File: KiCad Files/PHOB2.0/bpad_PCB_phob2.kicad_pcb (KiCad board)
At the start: 2 copper layers, 31.6 x 54.4 mm, 25 parts, among them J1 Conn_01x06, SW1 C_left, SW2 C_up, SW3 C_down, SW4 C_right, U1 MCP3202

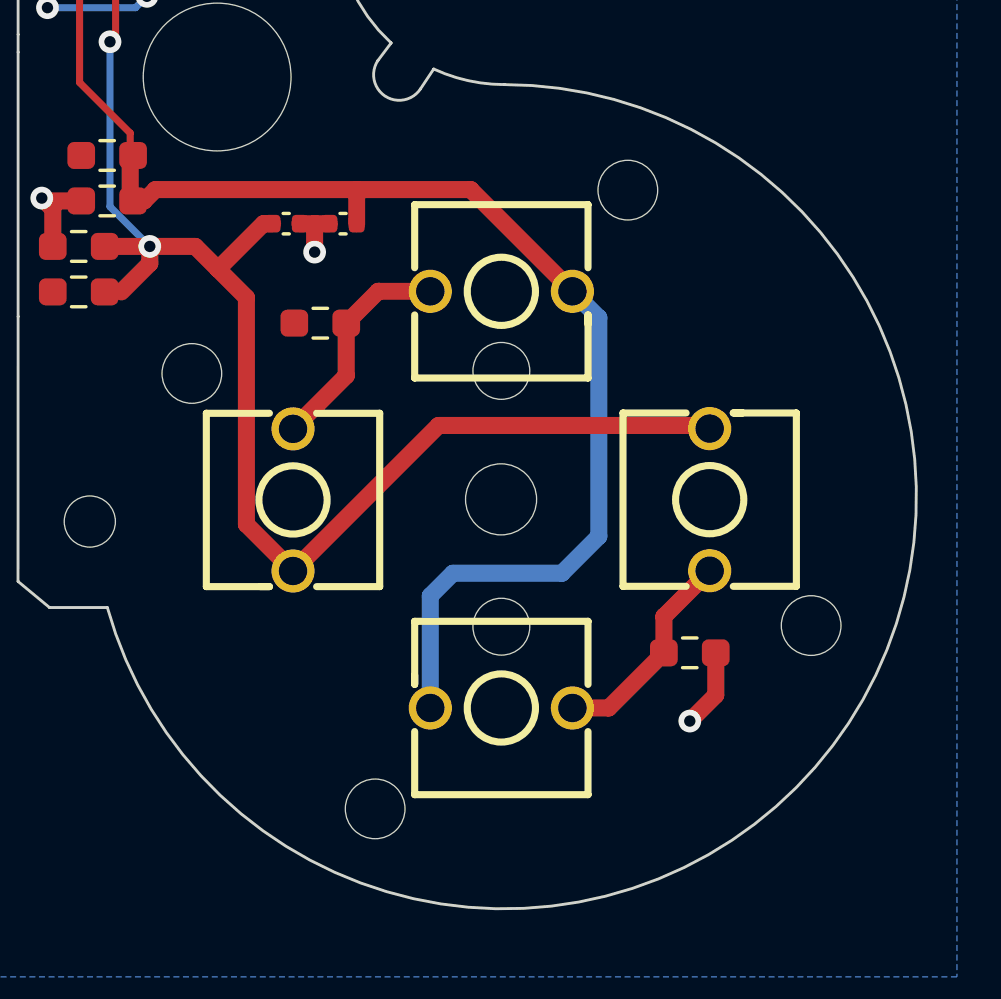
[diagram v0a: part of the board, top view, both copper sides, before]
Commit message: added gitignore and b3f support
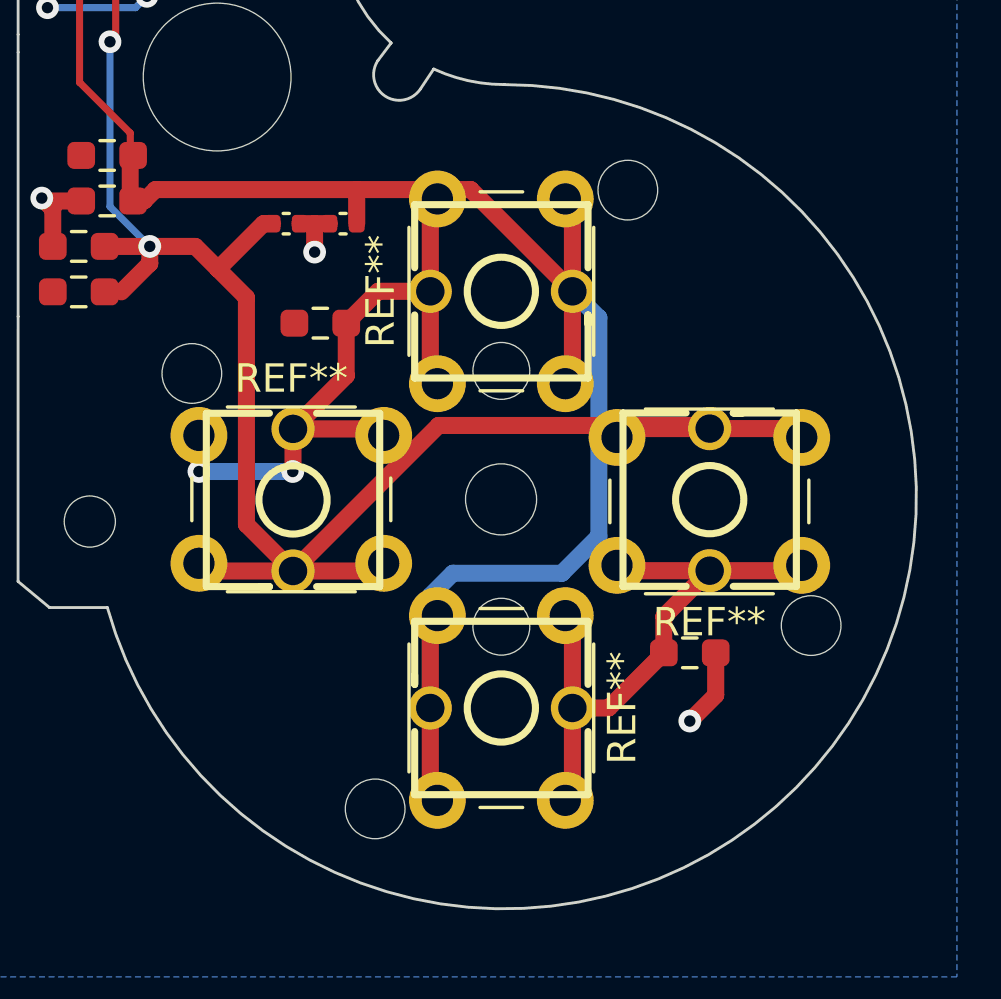
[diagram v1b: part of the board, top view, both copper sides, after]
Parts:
- added REF**: SW_PUSH_6mm, Button_Switch_THT:SW_PUSH_6mm, F.Cu at (146.9, 112.5)
- added REF**: SW_PUSH_6mm, Button_Switch_THT:SW_PUSH_6mm, F.Cu at (138.6, 114.3)
- added REF**: SW_PUSH_6mm, Button_Switch_THT:SW_PUSH_6mm, F.Cu at (125.7, 108.0)
- added REF**: SW_PUSH_6mm, Button_Switch_THT:SW_PUSH_6mm, F.Cu at (134.1, 106.1)
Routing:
- net Net-(SW2-Pad1): track 7.92 -> 23.6 mm, vias 0 -> 2
- net /C_y: track 48.5 -> 62.0 mm
- net /C_x: track 47.1 -> 60.5 mm
- net Net-(R1-Pad1): track 7.58 -> 20.9 mm

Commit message: Update bpad_PCB_phob2.kicad_pcb
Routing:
- net /C_x: track 60.5 -> 62.2 mm
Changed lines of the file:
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@@
     (tags "tact sw push 6mm")
     (attr through_hole)
-    (fp_text reference "REF**" (at 3.25 -2) (layer "F.SilkS")
+    (fp_text reference "REF**" (at 3.25 -2) (layer "F.SilkS") hide
         (effects (font (size 1 1) (thickness 0.15)))
     )
@@
     (tags "tact sw push 6mm")
     (attr through_hole)
-    (fp_text reference "REF**" (at 3.25 -2 90) (layer "F.SilkS")
+    (fp_text reference "REF**" (at 3.25 -2 90) (layer "F.SilkS") hide
         (effects (font (size 1 1) (thickness 0.15)))
     )
@@
     (tags "tact sw push 6mm")
     (attr through_hole)
-    (fp_text reference "REF**" (at 3.25 -2) (layer "F.SilkS")
+    (fp_text reference "REF**" (at 3.25 -2) (layer "F.SilkS") hide
         (effects (font (size 1 1) (thickness 0.15)))
     )
@@
     (tags "tact sw push 6mm")
     (attr through_hole)
-    (fp_text reference "REF**" (at 3.25 -2 90) (layer "F.SilkS")
+    (fp_text reference "REF**" (at 3.25 -2 90) (layer "F.SilkS") hide
         (effects (font (size 1 1) (thickness 0.15)))
     )
@@
   (segment (start 126 112.72) (end 125.73 112.45) (width 0.6) (layer "F.Cu") (net 2))
   (segment (start 129.04 112.72) (end 131.96 112.72) (width 0.6) (layer "F.Cu") (net 2))
+  (segment (start 143.59 107.6) (end 134.589 107.6) (width 0.6) (layer "F.Cu") (net 2))
   (segment (start 131.96 112.72) (end 132.23 112.45) (width 0.6) (layer "F.Cu") (net 2))
   (segment (start 143.7 107.71) (end 140.751 107.71) (width 0.6) (layer "F.Cu") (net 2))
   (segment (start 122.8 91.475) (end 122.8 93.9) (width 0.25) (layer "F.Cu") (net 2))
+  (segment (start 143.7 107.71) (end 143.59 107.6) (width 0.6) (layer "F.Cu") (net 2))
   (segment (start 124 101.3) (end 124 101.9) (width 0.6) (layer "F.Cu") (net 2))
   (segment (start 124 101.3) (end 122.4125 101.3) (width 0.6) (layer "F.Cu") (net 2))
-  (segment (start 134.16 107.6) (end 129.04 112.72) (width 0.6) (layer "F.Cu") (net 2))
   (segment (start 143.7 107.71) (end 146.627 107.71) (width 0.6) (layer "F.Cu") (net 2))
   (segment (start 128 100.5) (end 126.4 102.1) (width 0.6) (layer "F.Cu") (net 2))
-  (segment (start 143.7 107.71) (end 143.59 107.6) (width 0.6) (layer "F.Cu") (net 2))
-  (segment (start 143.59 107.6) (end 134.16 107.6) (width 0.6) (layer "F.Cu") (net 2))
+  (segment (start 134.589 107.6) (end 129.469 112.72) (width 0.6) (layer "F.Cu") (net 2))
   (segment (start 129.04 112.72) (end 127.4 111.08) (width 0.6) (layer "F.Cu") (net 2))
   (segment (start 126.4 102.1) (end 125.6 101.3) (width 0.6) (layer "F.Cu") (net 2))
@@
   (segment (start 129.04 112.72) (end 126 112.72) (width 0.6) (layer "F.Cu") (net 2))
   (segment (start 127.4 111.08) (end 127.4 103.1) (width 0.6) (layer "F.Cu") (net 2))
+  (segment (start 129.469 112.72) (end 129.04 112.72) (width 0.6) (layer "F.Cu") (net 2))
   (via (at 122.6 94.1) (size 0.8) (drill 0.4) (layers "F.Cu" "B.Cu") (net 2))
   (via (at 124 101.3) (size 0.8) (drill 0.4) (layers "F.Cu" "B.Cu") (net 2))
   (segment (start 122.6 99.9) (end 122.6 94.1) (width 0.25) (layer "B.Cu") (net 2))
   (segment (start 124 101.3) (end 122.6 99.9) (width 0.25) (layer "B.Cu") (net 2))
-  (segment (start 138.87 102.88) (end 135.29 99.3) (width 0.6) (layer "F.Cu") (net 3))
-  (segment (start 135.29 99.3) (end 124.2 99.3) (width 0.6) (layer "F.Cu") (net 3))
+  (segment (start 128.524 98.552) (end 124.948 98.552) (width 0.6) (layer "F.Cu") (net 3))
+  (segment (start 138.87 102.04) (end 134.62 97.79) (width 0.6) (layer "F.Cu") (net 3))
+  (segment (start 134.62 97.79) (end 129.286 97.79) (width 0.6) (layer "F.Cu") (net 3))
   (segment (start 123.4125 98.1) (end 123.3125 98.2) (width 0.6) (layer "F.Cu") (net 3))
   (segment (start 138.87 102.88) (end 138.87 99.88) (width 0.6) (layer "F.Cu") (net 3))
+  (segment (start 124.948 98.552) (end 123.8 99.7) (width 0.6) (layer "F.Cu") (net 3))
   (segment (start 133.87 117.54) (end 133.87 114.54) (width 0.6) (layer "F.Cu") (net 3))
   (segment (start 133.87 114.54) (end 134.12 114.29) (width 0.6) (layer "F.Cu") (net 3))
@@
   (segment (start 138.87 99.88) (end 138.62 99.63) (width 0.6) (layer "F.Cu") (net 3))
   (segment (start 138.87 102.88) (end 138.87 105.88) (width 0.6) (layer "F.Cu") (net 3))
-  (segment (start 124.2 99.3) (end 123.8 99.7) (width 0.6) (layer "F.Cu") (net 3))
+  (segment (start 123.8 99.7) (end 123.4125 99.7) (width 0.6) (layer "F.Cu") (net 3))
   (segment (start 133.87 120.54) (end 134.12 120.79) (width 0.6) (layer "F.Cu") (net 3))
   (segment (start 131.28 100.5) (end 131.28 99.3) (width 0.6) (layer "F.Cu") (net 3))
-  (segment (start 123.8 99.7) (end 123.4125 99.7) (width 0.6) (layer "F.Cu") (net 3))
   (segment (start 123.3125 98.2) (end 123.3125 99.7) (width 0.6) (layer "F.Cu") (net 3))
   (segment (start 121.53 95.53) (end 123.3125 97.3125) (width 0.25) (layer "F.Cu") (net 3))
+  (segment (start 129.286 97.79) (end 128.524 98.552) (width 0.6) (layer "F.Cu") (net 3))
   (segment (start 138.87 105.88) (end 138.62 106.13) (width 0.6) (layer "F.Cu") (net 3))
+  (segment (start 138.87 102.88) (end 138.87 102.04) (width 0.6) (layer "F.Cu") (net 3))
   (segment (start 123.3125 97.3125) (end 123.3125 98.1) (width 0.25) (layer "F.Cu") (net 3))
   (segment (start 133.87 117.54) (end 133.87 120.54) (width 0.6) (layer "F.Cu") (net 3))
